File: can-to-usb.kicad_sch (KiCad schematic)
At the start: 0 parts

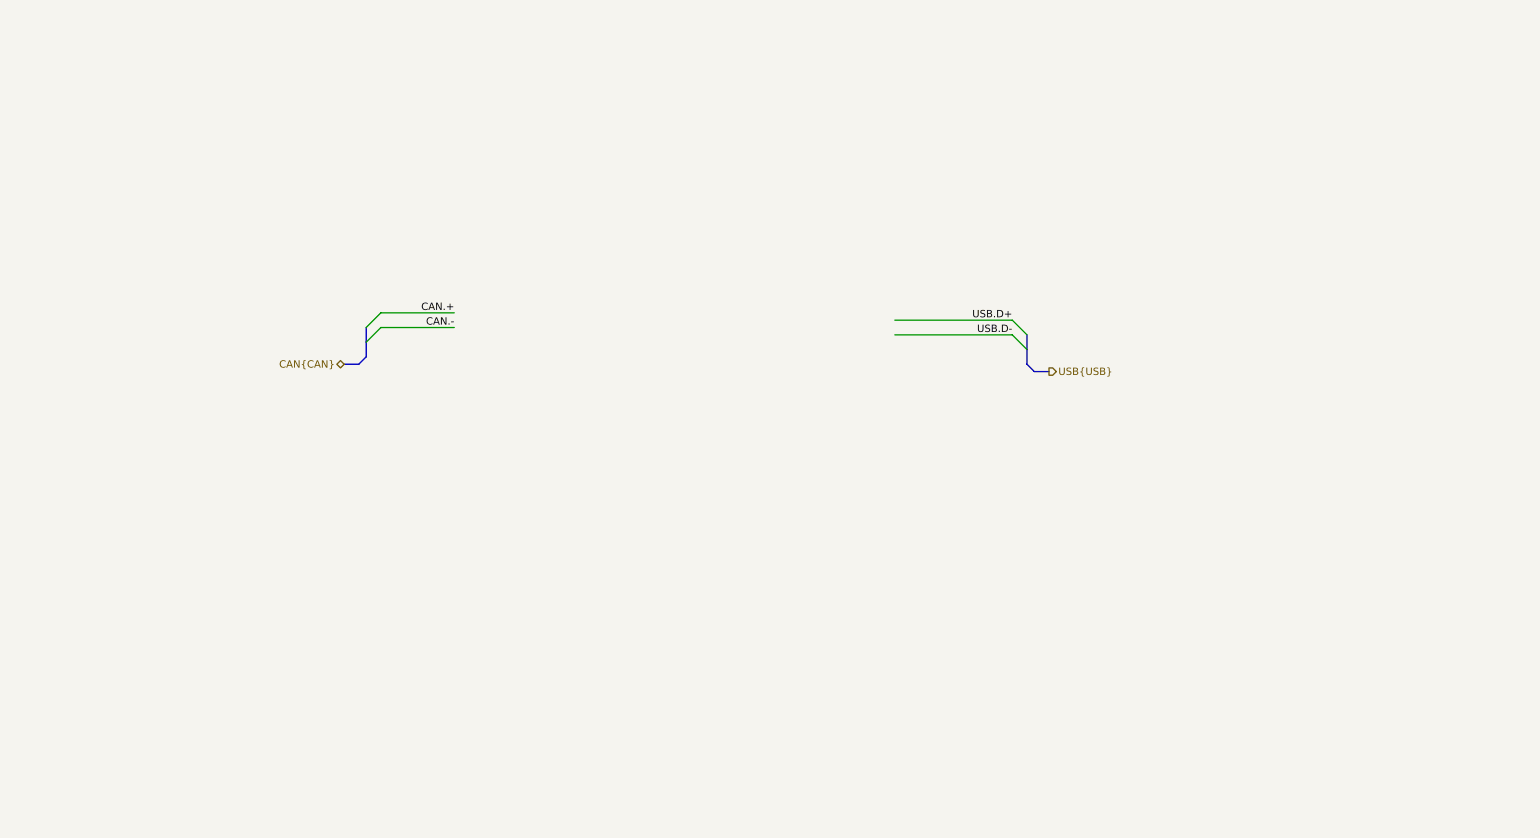
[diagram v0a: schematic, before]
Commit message: [#1] Add USB to CAN schematic, add power flags to 5V and 3V3
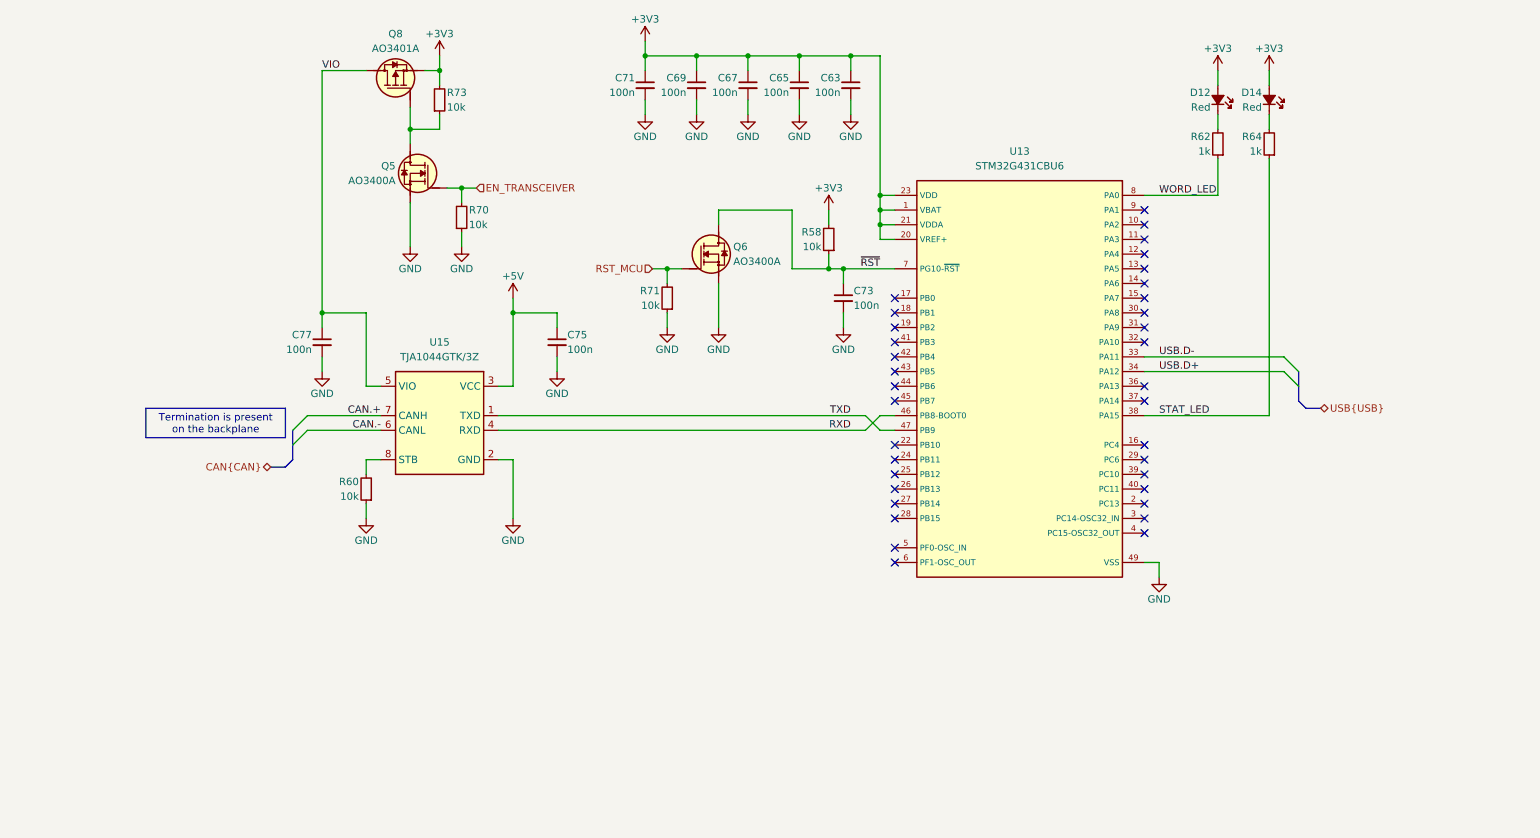
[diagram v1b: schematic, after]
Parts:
- added C63, C65, C67, C69, C71, C73, C75, C77: C-100n-0402, DW-footprints:C_0402_1005Metric, symbol DW-capacitors:C-100n-0402
- added D12, D14: LED-R-0603_KT-0603R, DW-footprints:LED_0603_1608Metric_R, symbol DW-diodes:LED-R-0603_KT-0603R
- added Q5, Q6: AO3400A, DW-footprints:SOT-23-3, symbol DW-transistors:AO3400A
- added Q8: AO3401A, DW-footprints:SOT-23-3, symbol DW-transistors:AO3401A
- added R58, R60, R70, R71, R73: R-10k-0402, DW-footprints:R_0402_1005Metric, symbol DW-resistors:R-10k-0402
- added R62, R64: R-1k-0402, DW-footprints:R_0402_1005Metric, symbol DW-resistors:R-1k-0402
- added U13: STM32G431CBU6, DW-footprints:UFQFPN-48-1EP_7x7mm_P0.5mm_EP5.7x5.7mm, symbol DW-ICs:STM32G431CBU6
- added U15: TJA1044GTK_3Z, DW-footprints:HVSON-8-1EP_3x3mm_P0.65mm_EP1.6x2.4mm, symbol DW-ICs:TJA1044GTK_3Z
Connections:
- net CAN.+: now also U15.7 (CANH)
- net CAN.-: now also U15.6 (CANL)
- net USB.D+: now also U13.34 (PA12)
- net USB.D-: now also U13.33 (PA11)
- new net: Q5.3 (D), Q8.1 (G), R73.1
- new net: D14.1 (C), R64.2
- new net: R60.2, U15.8 (STB)
- new net: D12.1 (C), R62.2
- new net +3V3: C63.1, C65.1, C67.1, C69.1, C71.1, D12.2 (A), D14.2 (A), Q8.2 (S), R58.2, R73.2, U13.1 (VBAT), U13.20 (VREF+), U13.21 (VDDA), U13.23 (VDD), U13.35 (VDD), U13.48 (VDD)
- new net +5V: C75.1, U15.3 (VCC)
- new net EN_TRANSCEIVER: Q5.1 (G), R70.2
- new net GND: C63.2, C65.2, C67.2, C69.2, C71.2, C73.2, C75.2, C77.2, Q5.2 (S), Q6.2 (S), R60.1, R70.1, R71.1, U13.49 (VSS), U15.2 (GND), U15.9 (GND)
- new net RST_MCU: Q6.1 (G), R71.2
- new net RXD: U13.46 (PB8-BOOT0), U15.4 (RXD)
- new net STAT_LED: R64.1, U13.38 (PA15)
- new net TXD: U13.47 (PB9), U15.1 (TXD)
- new net VIO: C77.1, Q8.3 (D), U15.5 (VIO)
- new net WORD_LED: R62.1, U13.8 (PA0)
- new net ~{RST}: C73.1, Q6.3 (D), R58.1, U13.7 (PG10-~{RST})
- no-connect marks 0 -> 35

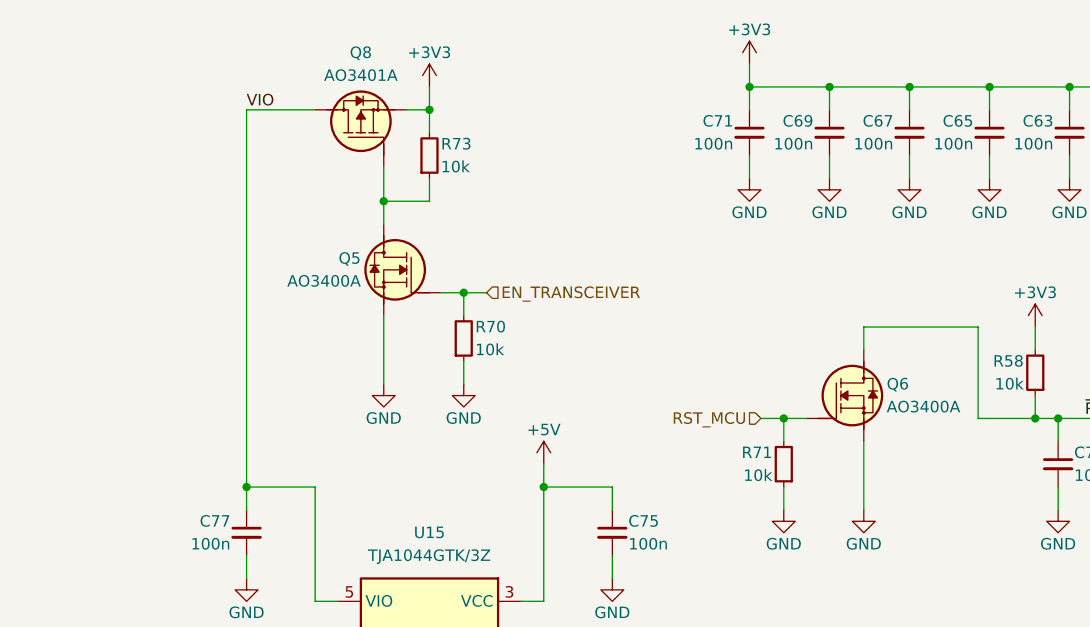
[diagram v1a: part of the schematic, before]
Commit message: [#1] Add USB switch and 0R to USB hub data lines, minor schematic refactor
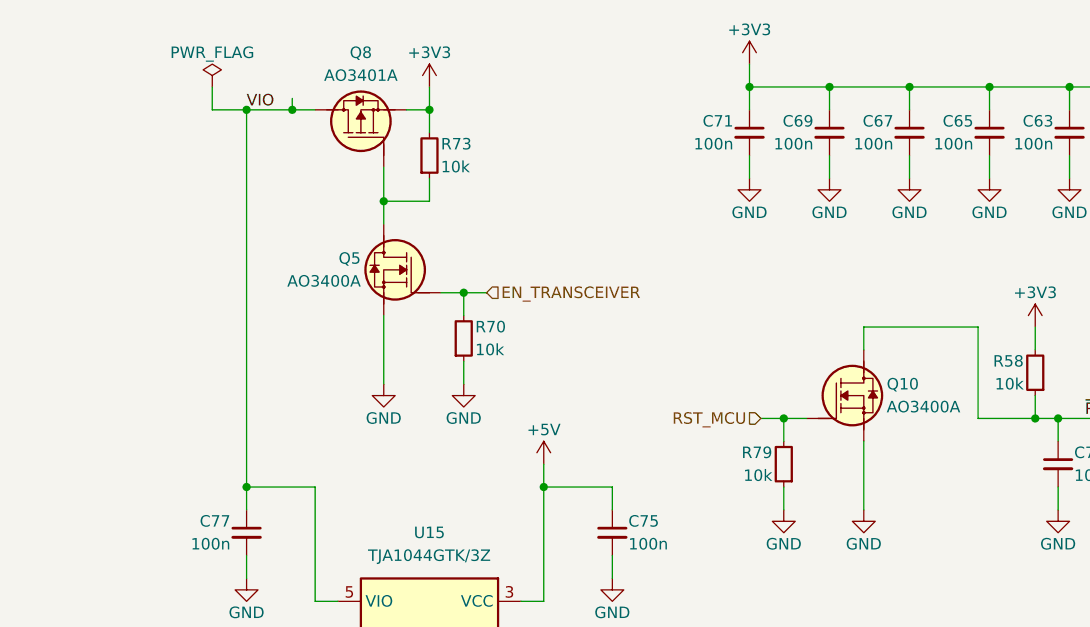
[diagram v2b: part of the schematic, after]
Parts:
- renumbered Q6 to Q10, R71 to R79
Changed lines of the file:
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@@
 	)
 	(junction
+		(at 73.66 57.15)
+		(diameter 0)
+		(color 0 0 0 0)
+	)
+	(junction
 		(at 170.18 81.28)
 		(diameter 0)
@@
 		(color 0 0 0 0)
 	)
+	(junction
+		(at 78.74 57.15)
+		(diameter 0)
+		(color 0 0 0 0)
+	)
 	(no_connect
 		(at 172.72 121.92)
@@
 	(wire
 		(pts
+			(xy 78.74 55.88) (xy 78.74 57.15)
+		)
+		(stroke
+			(width 0)
+			(type default)
+		)
+	)
+	(wire
+		(pts
 			(xy 170.18 116.84) (xy 172.72 116.84)
 		)
@@
 	(wire
 		(pts
+			(xy 73.66 57.15) (xy 78.74 57.15)
+		)
+		(stroke
+			(width 0)
+			(type default)
+		)
+	)
+	(wire
+		(pts
 			(xy 163.83 99.06) (xy 163.83 101.6)
 		)
@@
 		)
 	)
+	(wire
+		(pts
+			(xy 78.74 57.15) (xy 81.28 57.15)
+		)
+		(stroke
+			(width 0)
+			(type default)
+		)
+	)
 	(bus
 		(pts
@@
 		)
 	)
+	(wire
+		(pts
+			(xy 69.85 54.61) (xy 69.85 57.15)
+		)
+		(stroke
+			(width 0)
+			(type default)
+		)
+	)
 	(bus
 		(pts
@@
 	(wire
 		(pts
-			(xy 73.66 57.15) (xy 81.28 57.15)
-		)
-		(stroke
-			(width 0)
-			(type default)
-		)
-	)
-	(wire
-		(pts
 			(xy 170.18 78.74) (xy 170.18 81.28)
 		)
@@
 	(wire
 		(pts
+			(xy 69.85 57.15) (xy 73.66 57.15)
+		)
+		(stroke
+			(width 0)
+			(type default)
+		)
+	)
+	(wire
+		(pts
 			(xy 170.18 83.82) (xy 170.18 86.36)
 		)
@@
 		)
 	)
+	(netclass_flag ""
+		(length 2.54)
+		(shape round)
+		(at 78.74 55.88 0)
+		(effects
+			(font
+				(size 1.27 1.27)
+			)
+			(justify left bottom)
+		)
+		(property "Netclass" "PWR"
+			(at 78.74 51.054 0)
+			(effects
+				(font
+					(size 1.27 1.27)
+				)
+			)
+		)
+		(property "Component Class" ""
+			(at -172.72 -114.3 0)
+			(effects
+				(font
+					(size 1.27 1.27)
+					(italic yes)
+				)
+			)
+		)
+	)
 	(symbol
 		(lib_id "DW-power-symbols:GND")
@@
 	)
 	(symbol
+		(lib_id "DW-power-symbols:PWR_FLAG")
+		(at 69.85 54.61 0)
+		(unit 1)
+		(exclude_from_sim no)
+		(in_bom yes)
+		(on_board yes)
+		(dnp no)
+		(property "Reference" "#FLG011"
+			(at 69.85 52.705 0)
+			(effects
+				(font
+					(size 1.27 1.27)
+				)
+				(hide yes)
+			)
+		)
+		(property "Value" "PWR_FLAG"
+			(at 69.85 50.8 0)
+			(effects
+				(font
+					(size 1.27 1.27)
+				)
+			)
+		)
+		(property "Footprint" ""
+			(at 69.85 54.61 0)
+			(effects
+				(font
+					(size 1.27 1.27)
+				)
+				(hide yes)
+			)
+		)
+		(property "Datasheet" "~"
+			(at 69.85 54.61 0)
+			(effects
+				(font
+					(size 1.27 1.27)
+				)
+				(hide yes)
+			)
+		)
+		(property "Description" "Special symbol for telling ERC where power comes from"
+			(at 69.85 54.61 0)
+			(effects
+				(font
+					(size 1.27 1.27)
+				)
+				(hide yes)
+			)
+		)
+		(pin "1"
+		)
+		(instances
+			(project "cm5-module"
+				(path "/090a8e41-87a8-4fb1-998b-60a2c0dc4cee/1ecfee1b-3e5d-4e7d-896c-0cbef36fe0e5"
+					(reference "#FLG011")
+					(unit 1)
+				)
+				(path "/090a8e41-87a8-4fb1-998b-60a2c0dc4cee/f36d2c0d-933d-467c-b74d-11e2fa98d968"
+					(reference "#FLG012")
+					(unit 1)
+				)
+			)
+		)
+	)
+	(symbol
 		(lib_id "DW-ICs:STM32G431CBU6")
 		(at 215.9 78.74 0)
@@
 				)
 				(path "/090a8e41-87a8-4fb1-998b-60a2c0dc4cee/f36d2c0d-933d-467c-b74d-11e2fa98d968"
-					(reference "#PWR0168")
+					(reference "#PWR0187")
 					(unit 1)
 				)
@@
 		(on_board yes)
 		(dnp no)
-		(property "Reference" "R71"
+		(property "Reference" "R79"
 			(at 132.08 95.25 90)
 			(effects
@@
 			(project "cm5-module"
 				(path "/090a8e41-87a8-4fb1-998b-60a2c0dc4cee/1ecfee1b-3e5d-4e7d-896c-0cbef36fe0e5"
-					(reference "R71")
+					(reference "R79")
 					(unit 1)
 				)
@@
 		(on_board yes)
 		(dnp no)
-		(property "Reference" "Q6"
+		(property "Reference" "Q10"
 			(at 144.78 87.63 0)
 			(effects
@@
 			(project "cm5-module"
 				(path "/090a8e41-87a8-4fb1-998b-60a2c0dc4cee/1ecfee1b-3e5d-4e7d-896c-0cbef36fe0e5"
-					(reference "Q6")
+					(reference "Q10")
 					(unit 1)
 				)
@@
 				)
 				(path "/090a8e41-87a8-4fb1-998b-60a2c0dc4cee/f36d2c0d-933d-467c-b74d-11e2fa98d968"
-					(reference "#PWR0177")
+					(reference "#PWR0188")
 					(unit 1)
 				)

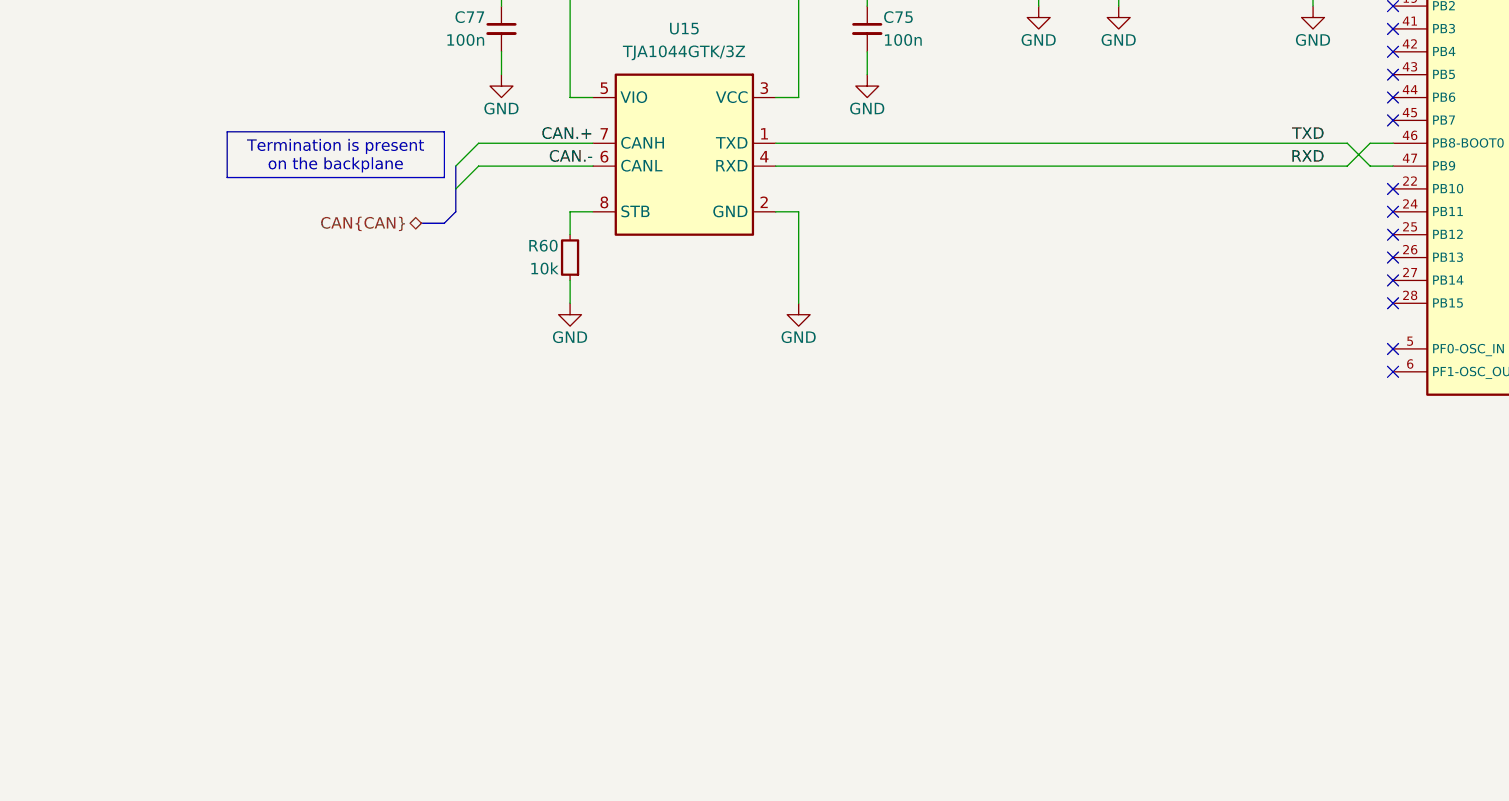
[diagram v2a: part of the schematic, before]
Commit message: [#3] Fix 3V3 DC-DC converter schematic, change one USB-C to a vertical one, start layout
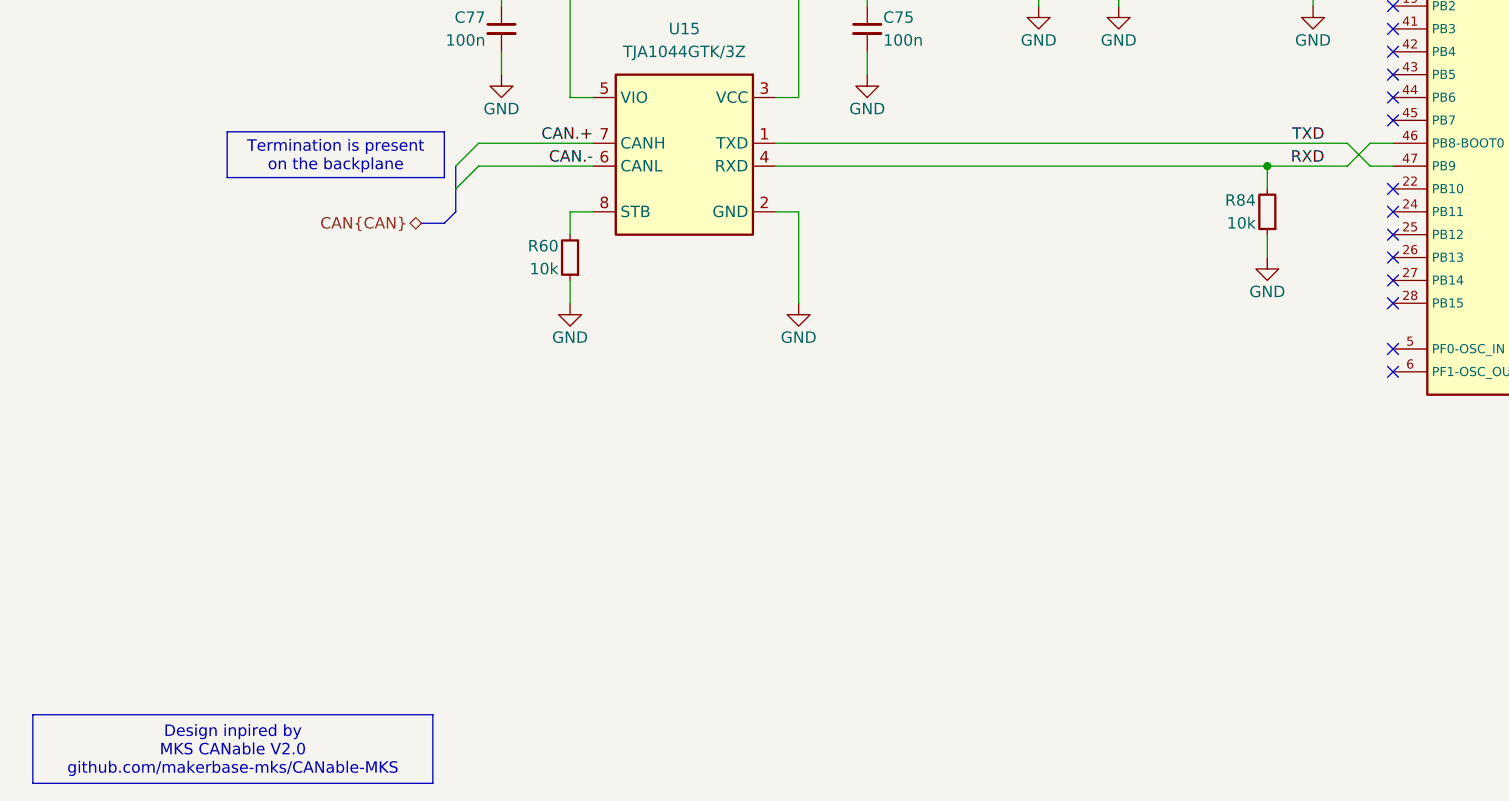
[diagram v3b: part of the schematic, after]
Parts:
- added R84: R-10k-0402, DW-footprints:R_0402_1005Metric, symbol DW-resistors:R-10k-0402
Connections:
- net GND: now also R84.1
- net RXD: now also R84.2
